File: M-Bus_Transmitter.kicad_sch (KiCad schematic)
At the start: 8 parts, among them J1 6P6C, U5 NCN5150DG

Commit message: Created Version 1.0
Refactored board with tipps after coaching
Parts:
- added C7: 100u, Capacitor_SMD:CP_Elec_6.3x7.7, symbol Steppermotor_Board-rescue:CP-Device
- R4: value 30k -> 4k
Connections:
- net GND: now also C7.2
- net at U5.3 (STC): now also C7.1
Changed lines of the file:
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@@
+    (stroke (width 0) (type default) (color 0 0 0 0))
+  )
+  (wire (pts (xy 105.41 83.82) (xy 105.41 104.14))
     (stroke (width 0) (type default) (color 0 0 0 0))
   )
@@
     (stroke (width 0) (type default) (color 0 0 0 0))
   )
+  (wire (pts (xy 140.97 83.82) (xy 105.41 83.82))
+    (stroke (width 0) (type default) (color 0 0 0 0))
+  )
   (wire (pts (xy 139.7 91.44) (xy 139.7 104.14))
+    (stroke (width 0) (type default) (color 0 0 0 0))
+  )
+  (wire (pts (xy 105.41 111.76) (xy 105.41 118.11))
     (stroke (width 0) (type default) (color 0 0 0 0))
   )
@@
     (pin "2")
   )
+  (symbol (lib_id "power:GND") (at 105.41 118.11 0) (unit 1)
+    (in_bom yes) (on_board yes) (fields_autoplaced)
+    (property "Reference" "#PWR06" (id 0) (at 105.41 124.46 0)
+      (effects (font (size 1.27 1.27)) hide)
+    )
+    (property "Value" "GND" (id 1) (at 105.41 122.5534 0))
+    (property "Footprint" "" (id 2) (at 105.41 118.11 0)
+      (effects (font (size 1.27 1.27)) hide)
+    )
+    (property "Datasheet" "" (id 3) (at 105.41 118.11 0)
+      (effects (font (size 1.27 1.27)) hide)
+    )
+    (pin "1")
+  )
+  (symbol (lib_id "Steppermotor_Board-rescue:CP-Device") (at 105.41 107.95 0) (unit 1)
+    (in_bom yes) (on_board yes)
+    (property "Reference" "C7" (id 0) (at 108.4072 106.7816 0)
+      (effects (font (size 1.27 1.27)) (justify left))
+    )
+    (property "Value" "100u" (id 1) (at 108.4072 109.093 0)
+      (effects (font (size 1.27 1.27)) (justify left))
+    )
+    (property "Footprint" "Capacitor_SMD:CP_Elec_6.3x7.7" (id 2) (at 106.3752 111.76 0)
+      (effects (font (size 1.27 1.27)) hide)
+    )
+    (property "Datasheet" "~" (id 3) (at 105.41 107.95 0)
+      (effects (font (size 1.27 1.27)) hide)
+    )
+    (pin "1")
+    (pin "2")
+  )
   (symbol (lib_id "power:GND") (at 191.77 118.11 0) (unit 1)
     (in_bom yes) (on_board yes) (fields_autoplaced)
@@
       (effects (font (size 1.27 1.27)) (justify left))
     )
-    (property "Value" "30k" (id 1) (at 126.492 106.807 0)
-      (effects (font (size 1.27 1.27)) (justify left))
-    )
+    (property "Value" "4k" (id 1) (at 126.492 106.807 0)
+      (effects (font (size 1.27 1.27)) (justify left))
+    )

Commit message: Updated docs and fixed bug
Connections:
- net +3.3V: no longer U5.11 (VDD)
- net TX_ESP32: no longer names the net of U5.13 (RXI)
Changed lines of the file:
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@@
 (kicad_sch (version 20211123) (generator eeschema)
   (paper "A4")
-  (junction (at 172.72 91.44) (diameter 0) (color 0 0 0 0)
-  )
   (junction (at 172.72 96.52) (diameter 0) (color 0 0 0 0)
   )
@@
     (stroke (width 0) (type default) (color 0 0 0 0))
   )
-  (wire (pts (xy 171.45 86.36) (xy 194.31 86.36))
-    (stroke (width 0) (type default) (color 0 0 0 0))
-  )
   (wire (pts (xy 191.77 81.28) (xy 171.45 81.28))
     (stroke (width 0) (type default) (color 0 0 0 0))
@@
     (stroke (width 0) (type default) (color 0 0 0 0))
   )
-  (wire (pts (xy 171.45 91.44) (xy 172.72 91.44))
-    (stroke (width 0) (type default) (color 0 0 0 0))
-  )
   (global_label "RX_ESP32" (shape input) (at 124.46 96.52 180) (fields_autoplaced)
     (effects (font (size 1.27 1.27)) (justify right))
@@
     )
   )
-  (global_label "TX_ESP32" (shape input) (at 194.31 86.36 0) (fields_autoplaced)
-    (effects (font (size 1.27 1.27)) (justify left))
-    (property "Intersheet References" "${INTERSHEET_REFS}" (id 0) (at 205.8266 86.2806 0)
-      (effects (font (size 1.27 1.27)) (justify left) hide)
-    )
-  )

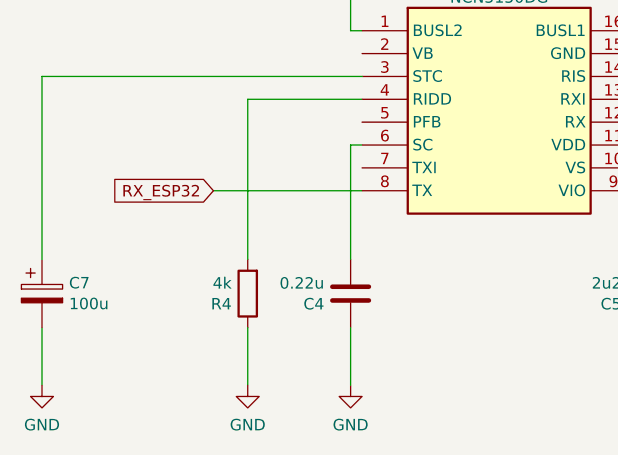
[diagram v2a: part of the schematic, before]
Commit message: Updated R4 Value and docs
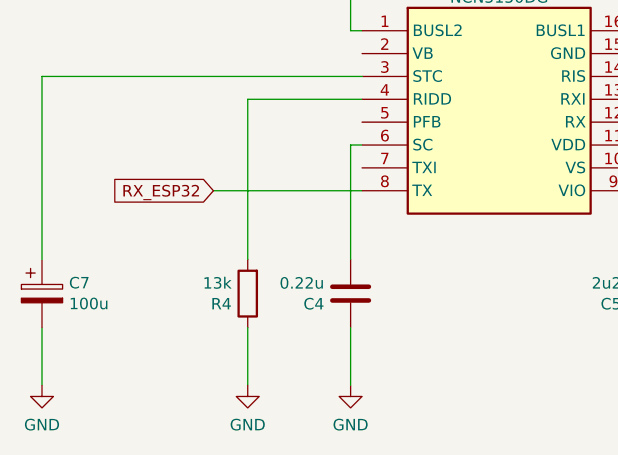
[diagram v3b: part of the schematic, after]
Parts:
- R4: value 4k -> 13k
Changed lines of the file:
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@@
       (effects (font (size 1.27 1.27)) (justify left))
     )
-    (property "Value" "4k" (id 1) (at 126.492 106.807 0)
+    (property "Value" "13k" (id 1) (at 126.492 106.807 0)
       (effects (font (size 1.27 1.27)) (justify left))
     )
